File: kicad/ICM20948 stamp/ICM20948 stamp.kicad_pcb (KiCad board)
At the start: 4 copper layers, 15.2 x 15.2 mm, 8 parts, among them U101 ICM-20948, U102 TXS0108EPW

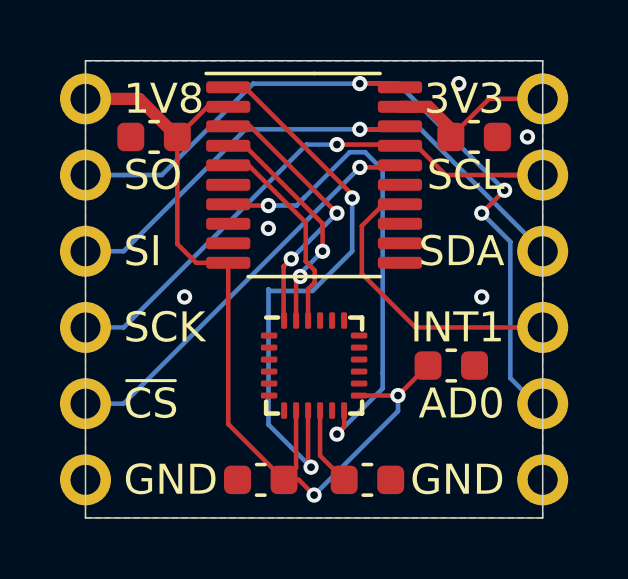
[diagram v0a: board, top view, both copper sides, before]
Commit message: Finished and decorated IMU stamp
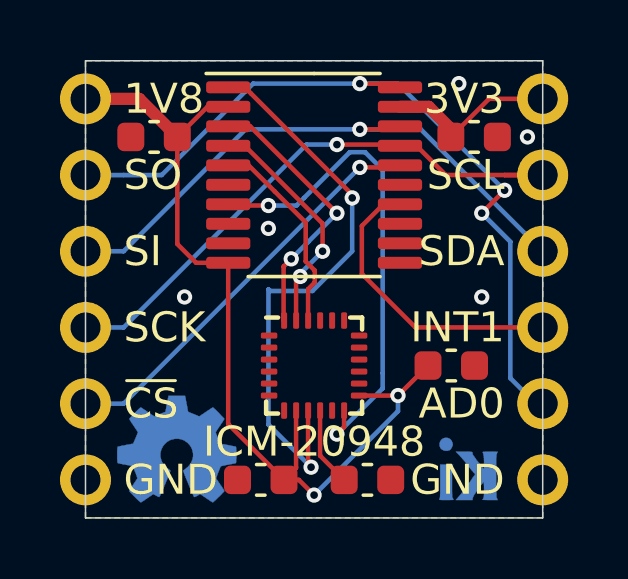
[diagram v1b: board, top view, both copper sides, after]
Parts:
- added G***: github.com/kwan3217, KwanSystems:KWAN_CIRCLE, B.Cu at (101.6, 101.6)
- added REF**: KiCAD Logo, KwanSystems:Symbol_KiCAD-Logo_CopperAndSilkScreenTop_small, B.Cu at (104.9, 107.7)
- added REF***: OSHW-Symbol_6.7x6mm_Copper, KwanSystems:OSHW-Symbol_4x3.6mm_SolderMask, B.Cu at (97.0, 106.9)
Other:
- board text added: "ICM20948 Stamp 01 Apr 2023"
